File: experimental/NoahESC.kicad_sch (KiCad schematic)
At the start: 48 parts, among them J1 5V, J10 GND, J12 PWM_IN, J2 12V, J3 GND, J7 DTR, J8 TX, J9 RX, Q1 IRLR7843TRPBF, Q2 IRLR7843TRPBF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

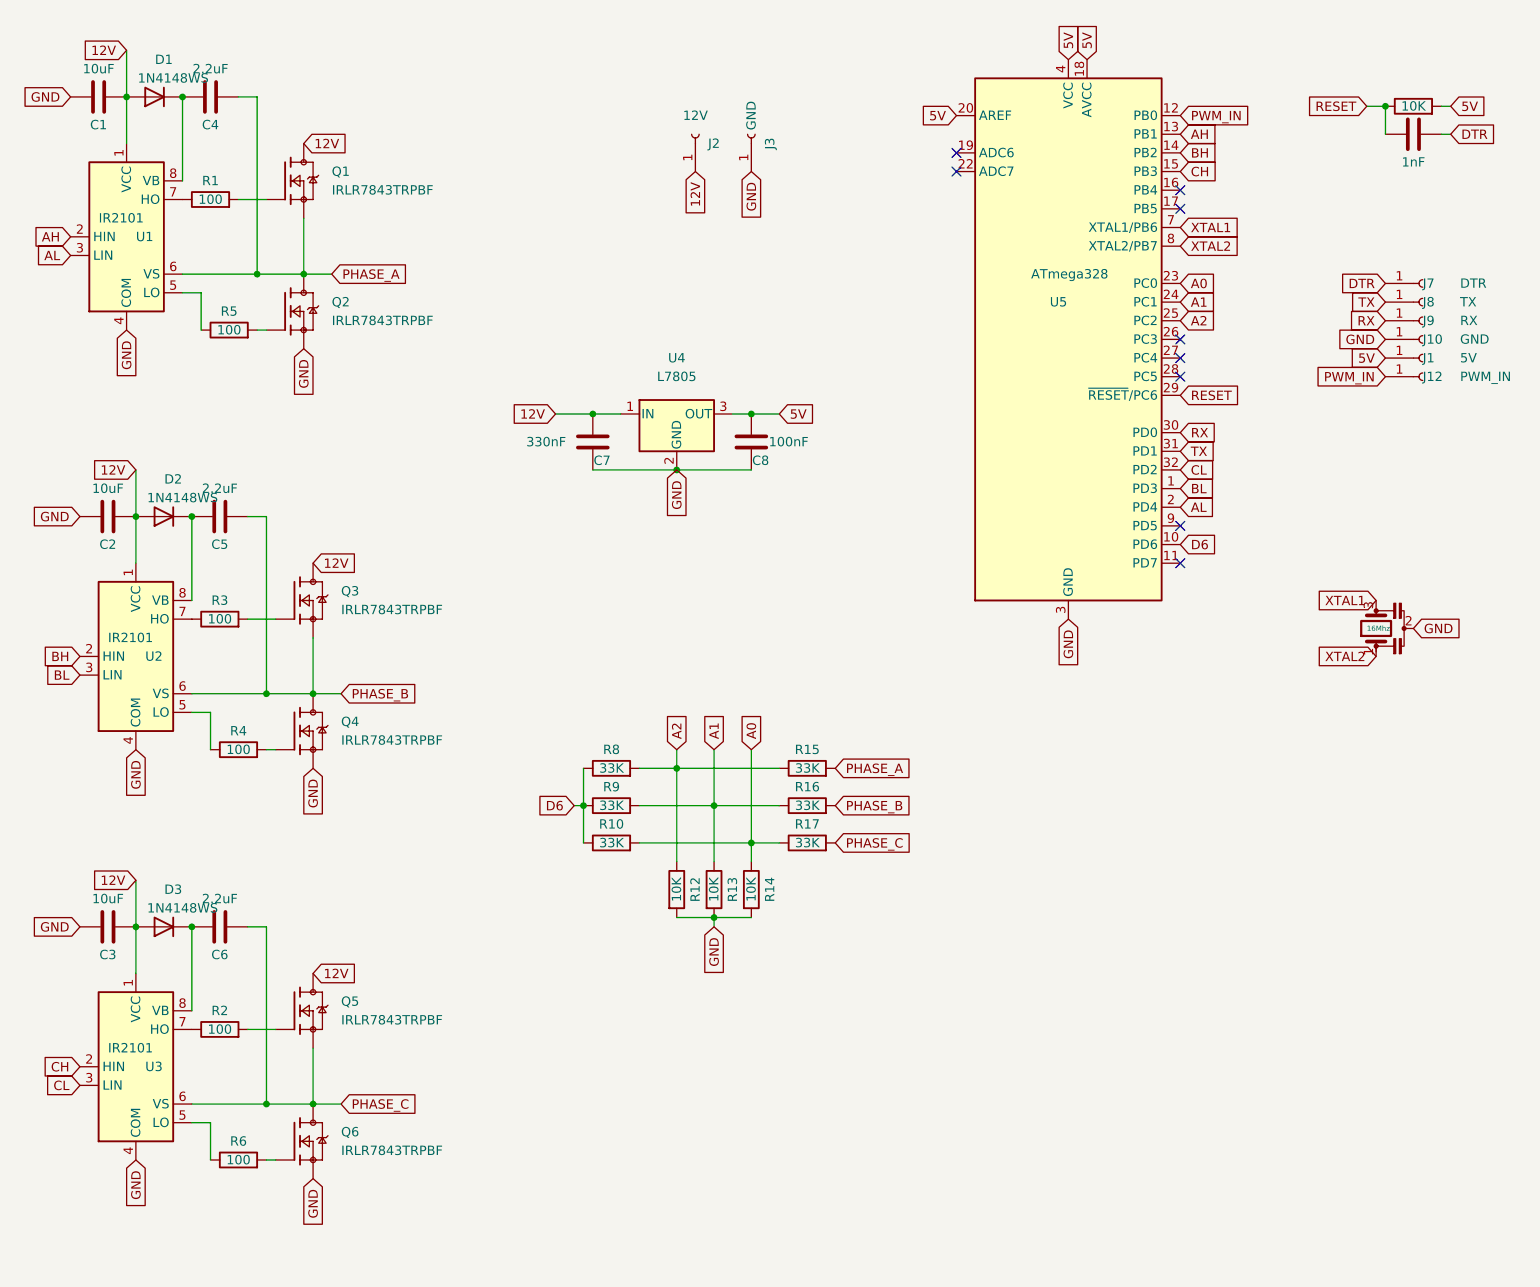
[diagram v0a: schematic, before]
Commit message: DIP version
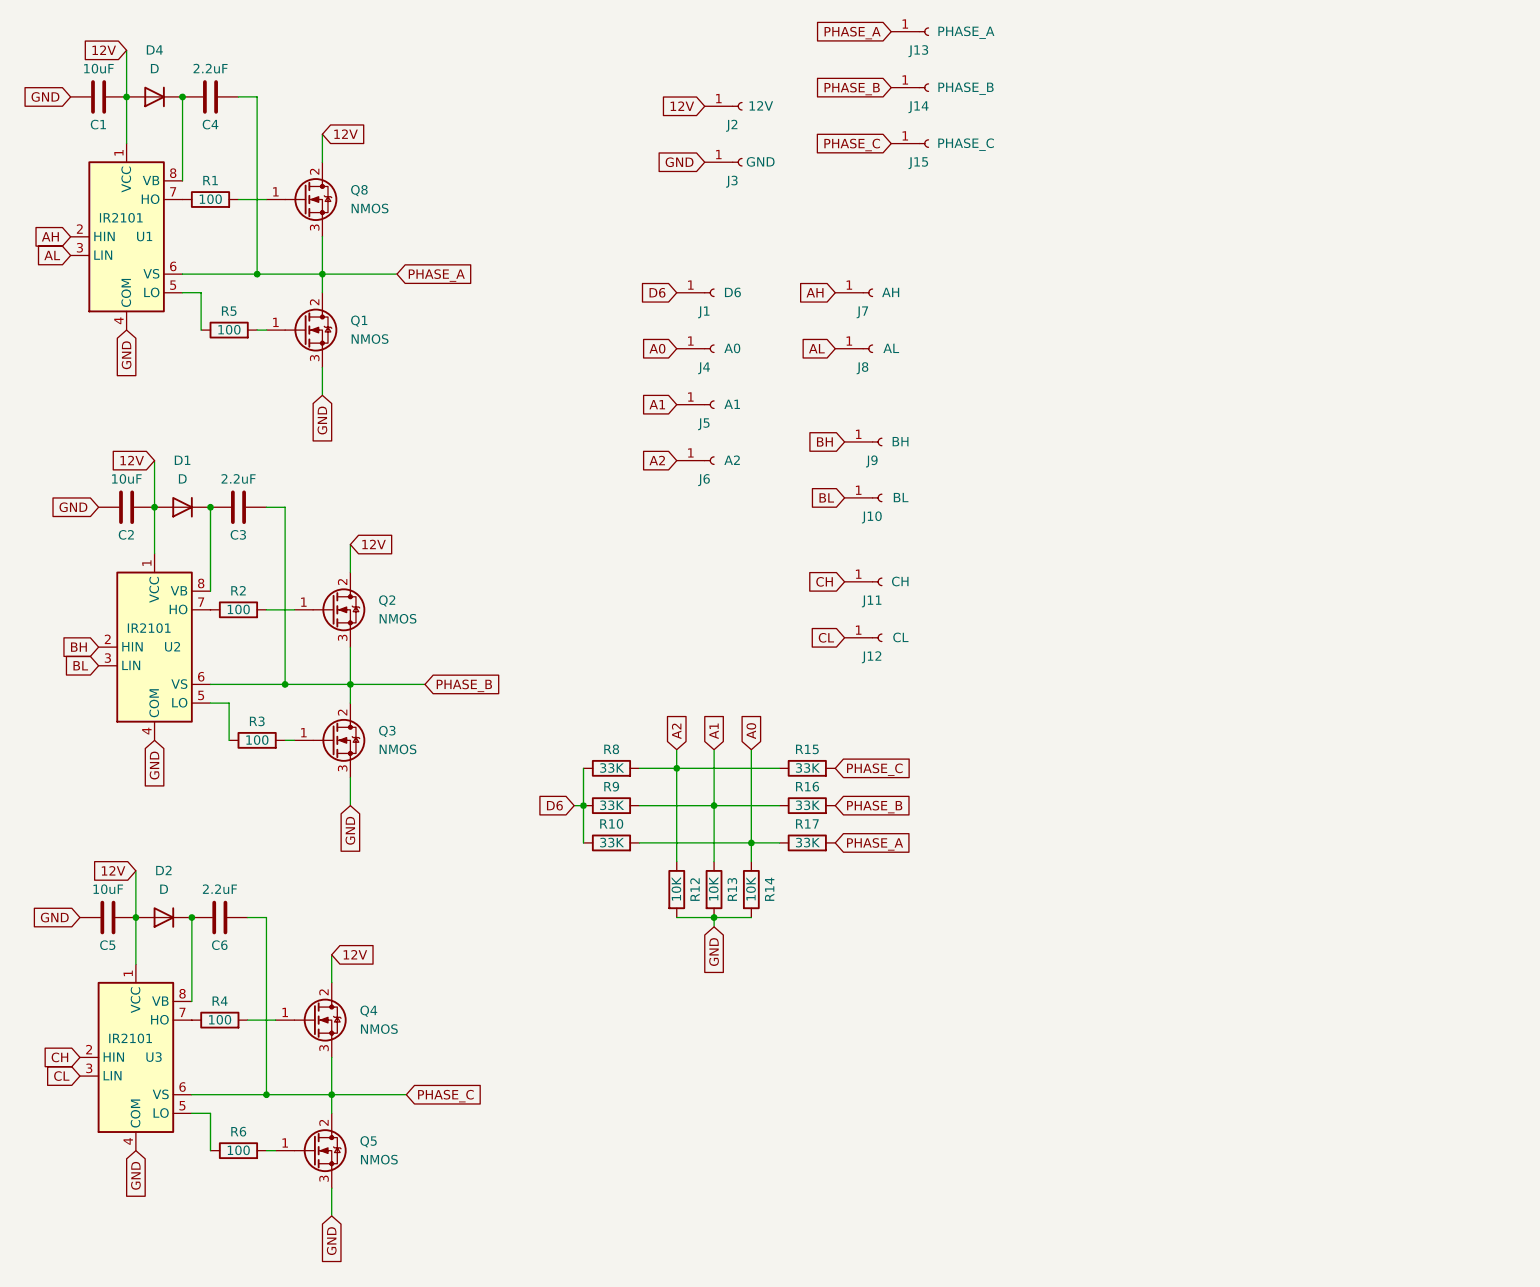
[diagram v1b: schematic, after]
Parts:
- removed C17: 1nF, Capacitor_SMD:C_0805_2012Metric, symbol Device:C
- removed C7: 330nF, Capacitor_SMD:C_0805_2012Metric, symbol Device:C
- removed C8: 100nF, Capacitor_SMD:C_0805_2012Metric, symbol Device:C
- removed D1, D2, D3: 1N4148WS, Diode_SMD:D_SOD-323, symbol Diode:1N4148WS
- removed J1: 5V, Connector_Wire:SolderWirePad_1x01_SMD_1x2mm, symbol Connector:Conn_01x01_Female
- removed J10: GND, Connector_Wire:SolderWirePad_1x01_SMD_1x2mm, symbol Connector:Conn_01x01_Female
- removed J12: PWM_IN, Connector_Wire:SolderWirePad_1x01_SMD_1x2mm, symbol Connector:Conn_01x01_Female
- removed J7: DTR, Connector_Wire:SolderWirePad_1x01_SMD_1x2mm, symbol Connector:Conn_01x01_Female
- removed J8: TX, Connector_Wire:SolderWirePad_1x01_SMD_1x2mm, symbol Connector:Conn_01x01_Female
- removed J9: RX, Connector_Wire:SolderWirePad_1x01_SMD_1x2mm, symbol Connector:Conn_01x01_Female
- removed Q1, Q2, Q3, Q4, Q5, Q6: IRLR7843TRPBF, TO229P990X239-3_4N, symbol IRLR7843TRPBF:IRLR7843TRPBF
- removed R20: 10K, Resistor_SMD:R_0805_2012Metric, symbol Device:R
- removed U4: L7805, Package_TO_SOT_SMD:SOT-89-3_Handsoldering, symbol Regulator_Linear:L7805
- removed U5: ATmega328, Package_QFP:TQFP-32_7x7mm_P0.8mm, symbol MCU_Microchip_ATmega:ATmega328-A
- removed Y1: 16Mhz, Crystal:Resonator_SMD_Murata_CSTxExxV-3Pin_3.0x1.1mm, symbol Device:Resonator
- added D1, D2, D4: D, Diode_THT:D_A-405_P7.62mm_Horizontal, symbol Device:D
- added J1: D6, Connector_PinHeader_2.54mm:PinHeader_1x01_P2.54mm_Vertical, symbol Connector:Conn_01x01_Socket
- added J10: BL, Connector_PinHeader_2.54mm:PinHeader_1x01_P2.54mm_Vertical, symbol Connector:Conn_01x01_Socket
- added J11: CH, Connector_PinHeader_2.54mm:PinHeader_1x01_P2.54mm_Vertical, symbol Connector:Conn_01x01_Socket
- added J12: CL, Connector_PinHeader_2.54mm:PinHeader_1x01_P2.54mm_Vertical, symbol Connector:Conn_01x01_Socket
- added J13: PHASE_A, TestPoint:TestPoint_Pad_3.0x3.0mm, symbol Connector:Conn_01x01_Socket
- added J14: PHASE_B, TestPoint:TestPoint_Pad_3.0x3.0mm, symbol Connector:Conn_01x01_Socket
- added J15: PHASE_C, TestPoint:TestPoint_Pad_3.0x3.0mm, symbol Connector:Conn_01x01_Socket
- added J4: A0, Connector_PinHeader_2.54mm:PinHeader_1x01_P2.54mm_Vertical, symbol Connector:Conn_01x01_Socket
- added J5: A1, Connector_PinHeader_2.54mm:PinHeader_1x01_P2.54mm_Vertical, symbol Connector:Conn_01x01_Socket
- added J6: A2, Connector_PinHeader_2.54mm:PinHeader_1x01_P2.54mm_Vertical, symbol Connector:Conn_01x01_Socket
- added J7: AH, Connector_PinHeader_2.54mm:PinHeader_1x01_P2.54mm_Vertical, symbol Connector:Conn_01x01_Socket
- added J8: AL, Connector_PinHeader_2.54mm:PinHeader_1x01_P2.54mm_Vertical, symbol Connector:Conn_01x01_Socket
- added J9: BH, Connector_PinHeader_2.54mm:PinHeader_1x01_P2.54mm_Vertical, symbol Connector:Conn_01x01_Socket
- added Q1, Q2, Q3, Q4, Q5, Q8: NMOS, Package_TO_SOT_THT:TO-220-3_Vertical, symbol Transistor_FET:BUZ11
- C1, C2, C4, C6: footprint Capacitor_SMD:C_0805_2012Metric -> Capacitor_THT:C_Axial_L5.1mm_D3.1mm_P7.50mm_Horizontal
- C3: value 10uF -> 2.2uF; footprint Capacitor_SMD:C_0805_2012Metric -> Capacitor_THT:C_Axial_L5.1mm_D3.1mm_P7.50mm_Horizontal
- C5: value 2.2uF -> 10uF; footprint Capacitor_SMD:C_0805_2012Metric -> Capacitor_THT:C_Axial_L5.1mm_D3.1mm_P7.50mm_Horizontal
- J2, J3: symbol Connector:Conn_01x01_Female -> Connector:Conn_01x01_Socket
- R1, R10, R12, R13, R14, R15, R16, R17, R2, R3, R4, R5, R6, R8, R9: footprint Resistor_SMD:R_0805_2012Metric -> Resistor_THT:R_Axial_DIN0207_L6.3mm_D2.5mm_P7.62mm_Horizontal
- U1, U2, U3: footprint Package_SO:SOIC-8_3.9x4.9mm_P1.27mm -> Package_DIP:DIP-8_W7.62mm_Socket
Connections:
- net 12V: now also C5.2, D1.2 (A), D2.2 (A), D4.2 (A), Q2.2 (D), Q4.2 (D), Q8.2 (D); no longer C3.2
- net A0: now also J4.1 (Pin_1)
- net A1: now also J5.1 (Pin_1)
- net A2: now also J6.1 (Pin_1)
- net AH: now also J7.1 (Pin_1)
- net AL: now also J8.1 (Pin_1)
- net BH: now also J9.1 (Pin_1)
- net BL: now also J10.1 (Pin_1)
- net CH: now also J11.1 (Pin_1)
- net CL: now also J12.1 (Pin_1)
- net D6: now also J1.1 (Pin_1)
- net GND: now also C5.1, Q1.3 (S), Q3.3 (S), Q5.3 (S); no longer C3.1
- net PHASE_A: now also R17.2, J13.1 (Pin_1), Q1.2 (D), Q8.3 (S); no longer R15.2
- net PHASE_B: now also C3.2, J14.1 (Pin_1), Q2.3 (S), Q3.2 (D); no longer C5.2
- net PHASE_C: now also R15.2, J15.1 (Pin_1), Q4.3 (S), Q5.2 (D); no longer R17.2
- net at U2.7 (HO): now also R2.1; no longer R3.1
- net at R3.2: now also Q3.1 (G)
- net at R4.2: now also Q4.1 (G)
- net at C4.1, U1.8 (VB): now also D4.1 (K)
- net at U2.8 (VB): now also C3.1, D1.1 (K); no longer C5.1
- net at R6.2: now also Q5.1 (G)
- net at U3.7 (HO): now also R4.1; no longer R2.1
- net at R2.2: now also Q2.1 (G)
- net at C6.1, U3.8 (VB): now also D2.1 (K)
- net at R5.2: now also Q1.1 (G)
- net at R1.2: now also Q8.1 (G)
- net at U2.5 (LO): now also R3.1; no longer R4.1
- no-connect marks 9 -> 0
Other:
- moved on the sheet: J2, J3
